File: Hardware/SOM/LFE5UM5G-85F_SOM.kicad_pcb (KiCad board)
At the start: 6 copper layers, 67.6 x 25.4 mm, 42 parts, among them J1 SODIMM-200_Split, U1 LFE5UM5G-85F, U2 AS4C256M16D3, U3 TLV62569DBV, U4 W25Q128JVP

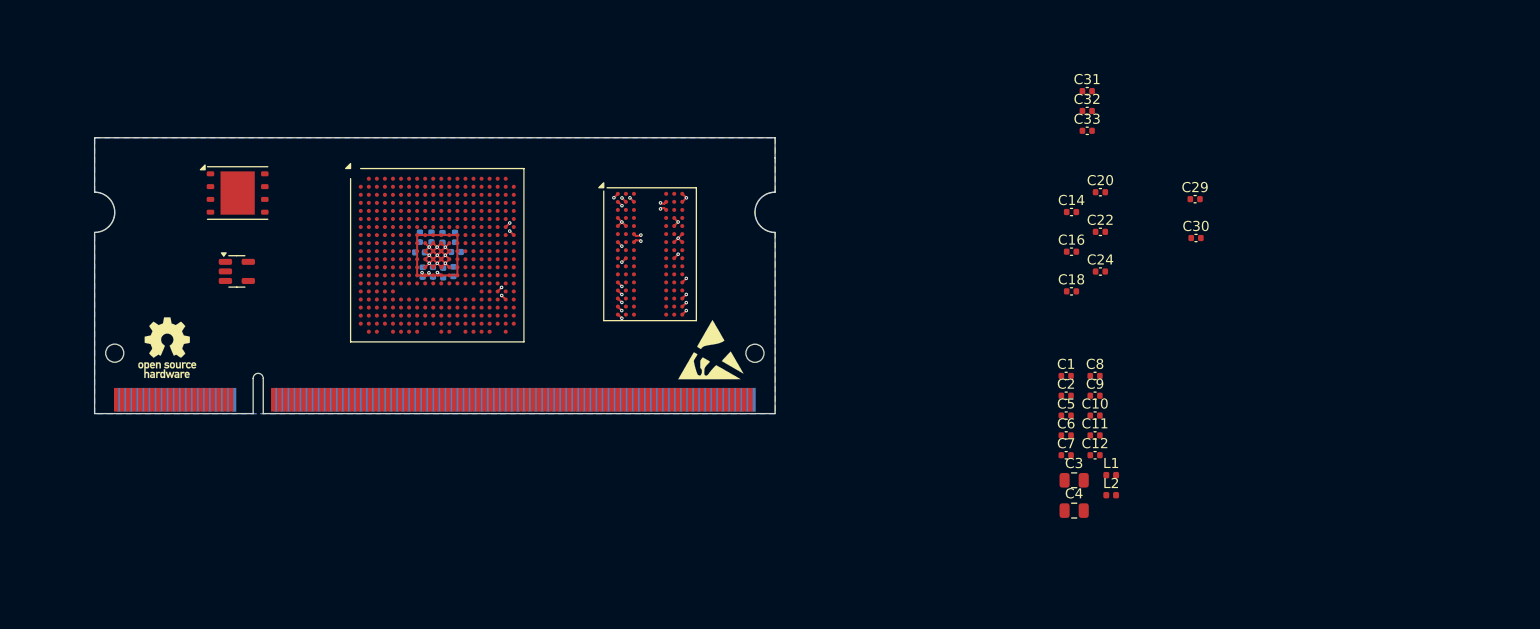
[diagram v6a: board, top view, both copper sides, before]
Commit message: SOM: power supply update
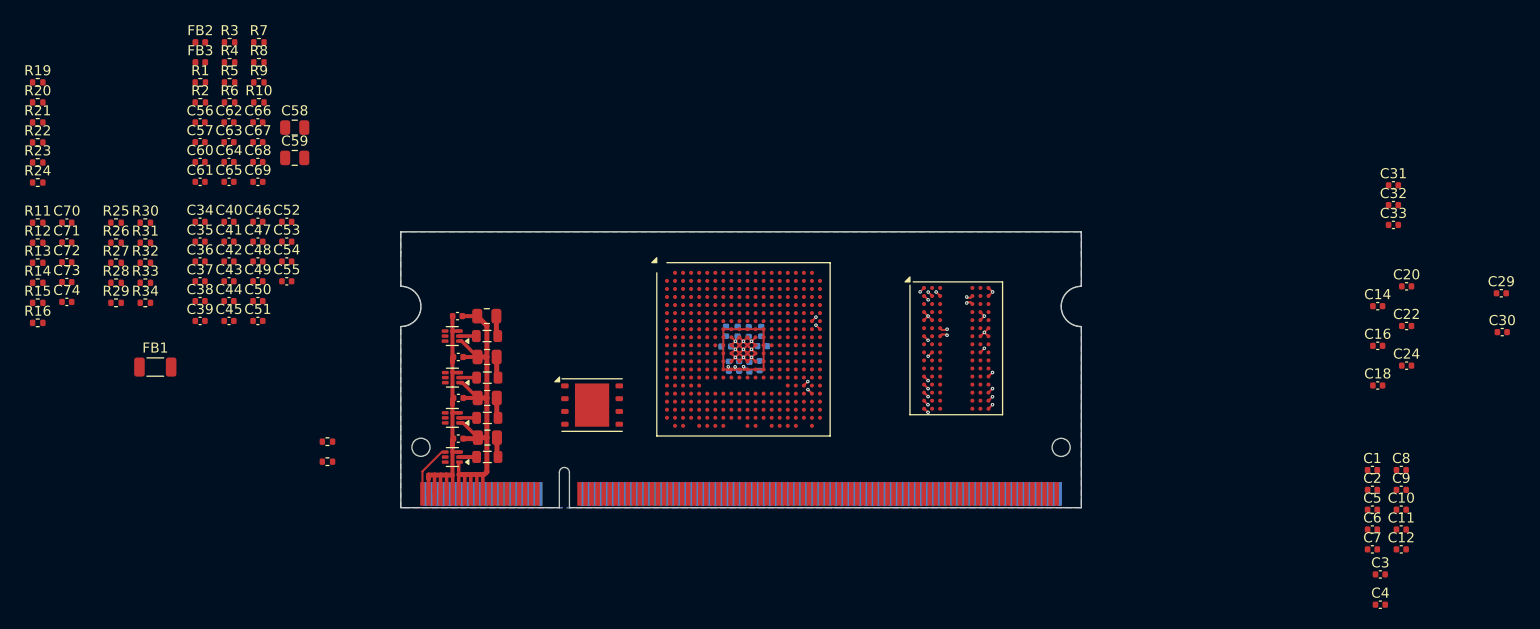
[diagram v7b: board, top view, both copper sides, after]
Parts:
- removed REF**: OSHW-Logo_5.7x6mm_SilkScreen, Symbol:OSHW-Logo_5.7x6mm_SilkScreen
- removed REF**: ESD-Logo_6.6x6mm_SilkScreen, Symbol:ESD-Logo_6.6x6mm_SilkScreen
- added C34: 100nF, Capacitor_SMD:C_0402_1005Metric, F.Cu at (61.9, 58.0)
- added C35: 10uF, Capacitor_SMD:C_0402_1005Metric, F.Cu at (61.9, 59.9)
- added C36: 10uF, Capacitor_SMD:C_0402_1005Metric, F.Cu at (61.9, 61.9)
- added C37: 10uF, Capacitor_SMD:C_0402_1005Metric, F.Cu at (61.9, 63.9)
- added C38: 10uF, Capacitor_SMD:C_0402_1005Metric, F.Cu at (61.9, 65.8)
- added C39: 10uF, Capacitor_SMD:C_0402_1005Metric, F.Cu at (61.9, 67.8)
- added C40: 1uF, Capacitor_SMD:C_0402_1005Metric, F.Cu at (64.8, 58.0)
- added C41: 100nF, Capacitor_SMD:C_0402_1005Metric, F.Cu at (64.8, 59.9)
- added C42: 100nF, Capacitor_SMD:C_0402_1005Metric, F.Cu at (64.8, 61.9)
- added C43: 1uF, Capacitor_SMD:C_0402_1005Metric, F.Cu at (64.8, 63.9)
- added C44: 100nF, Capacitor_SMD:C_0402_1005Metric, F.Cu at (64.8, 65.8)
- added C45: 100nF, Capacitor_SMD:C_0402_1005Metric, F.Cu at (64.8, 67.8)
- added C46: 100nF, Capacitor_SMD:C_0402_1005Metric, F.Cu at (67.7, 58.0)
- added C47: 100nF, Capacitor_SMD:C_0402_1005Metric, F.Cu at (67.7, 59.9)
- added C48: 1uF, Capacitor_SMD:C_0402_1005Metric, F.Cu at (67.7, 61.9)
- added C49: 100nF, Capacitor_SMD:C_0402_1005Metric, F.Cu at (67.7, 63.9)
- added C50: 100nF, Capacitor_SMD:C_0402_1005Metric, F.Cu at (67.7, 65.8)
- added C51: 100nF, Capacitor_SMD:C_0402_1005Metric, F.Cu at (67.7, 67.8)
- added C52: 100nF, Capacitor_SMD:C_0402_1005Metric, F.Cu at (70.5, 58.0)
- added C53: 100nF, Capacitor_SMD:C_0402_1005Metric, F.Cu at (70.5, 59.9)
- added C54: 10uF, Capacitor_SMD:C_0402_1005Metric, F.Cu at (70.5, 61.9)
- added C55: 10uF, Capacitor_SMD:C_0402_1005Metric, F.Cu at (70.5, 63.9)
- added C56: 100nF, Capacitor_SMD:C_0402_1005Metric, F.Cu at (61.9, 48.1)
- added C57: 100nF, Capacitor_SMD:C_0402_1005Metric, F.Cu at (61.9, 50.1)
- added C58: 22uF, Capacitor_SMD:C_0805_2012Metric, F.Cu at (71.3, 48.6)
- added C59: 22uF, Capacitor_SMD:C_0805_2012Metric, F.Cu at (71.3, 51.6)
- added C60: 1uF, Capacitor_SMD:C_0402_1005Metric, F.Cu at (61.9, 52.0)
- added C61: 1uF, Capacitor_SMD:C_0402_1005Metric, F.Cu at (61.9, 54.0)
- added C62: 1uF, Capacitor_SMD:C_0402_1005Metric, F.Cu at (64.8, 48.1)
- added C63: 1uF, Capacitor_SMD:C_0402_1005Metric, F.Cu at (64.8, 50.1)
- added C64: 100nF, Capacitor_SMD:C_0402_1005Metric, F.Cu at (64.8, 52.0)
- added C65: 100nF, Capacitor_SMD:C_0402_1005Metric, F.Cu at (64.8, 54.0)
- added C66: 100nF, Capacitor_SMD:C_0402_1005Metric, F.Cu at (67.7, 48.1)
- added C67: 100nF, Capacitor_SMD:C_0402_1005Metric, F.Cu at (67.7, 50.1)
- added C68: 1uF, Capacitor_SMD:C_0402_1005Metric, F.Cu at (67.7, 52.0)
- added C69: 100nF, Capacitor_SMD:C_0402_1005Metric, F.Cu at (67.7, 54.0)
- added C70: 22pF, Capacitor_SMD:C_0402_1005Metric, F.Cu at (48.7, 58.0)
- added C71: 22pF, Capacitor_SMD:C_0402_1005Metric, F.Cu at (48.7, 60.0)
- added C72: 22pF, Capacitor_SMD:C_0402_1005Metric, F.Cu at (48.7, 62.0)
- added C73: 100nF, Capacitor_SMD:C_0402_1005Metric, F.Cu at (48.7, 64.0)
- added C74: 10uF, Capacitor_SMD:C_0402_1005Metric, F.Cu at (48.7, 65.9)
- added C75: 10uF, Capacitor_SMD:C_0402_1005Metric, F.Cu at (87.6, 79.5)
- added C76: 10uF, Capacitor_SMD:C_0402_1005Metric, F.Cu at (87.6, 75.5)
- added C77: 22uF, Capacitor_SMD:C_0805_2012Metric, F.Cu at (90.5, 79.4)
- added C78: 22uF, Capacitor_SMD:C_0805_2012Metric, F.Cu at (90.5, 75.5)
- added C79: 10uF, Capacitor_SMD:C_0402_1005Metric, F.Cu at (87.6, 71.4)
- added C80: 10uF, Capacitor_SMD:C_0402_1005Metric, F.Cu at (87.5, 67.3)
- added C81: 22uF, Capacitor_SMD:C_0805_2012Metric, F.Cu at (90.4, 71.4)
- added C82: 22uF, Capacitor_SMD:C_0805_2012Metric, F.Cu at (90.4, 67.3)
- added FB1: FerriteBead, Inductor_SMD:L_1206_3216Metric, F.Cu at (57.5, 72.4)
- added FB2: FerriteBead, Inductor_SMD:L_0402_1005Metric, F.Cu at (62.0, 40.1)
- added FB3: FerriteBead, Inductor_SMD:L_0402_1005Metric, F.Cu at (62.0, 42.1)
- added L3: 1uH, Inductor_SMD:L_0805_2012Metric, F.Cu at (90.5, 73.5)
- added L4: 1uH, Inductor_SMD:L_0805_2012Metric, F.Cu at (90.4, 69.3)
- added R1: 100R, Resistor_SMD:R_0402_1005Metric, F.Cu at (62.0, 44.1)
- added R10: 1K, Resistor_SMD:R_0402_1005Metric, F.Cu at (67.8, 46.1)
- added R11: 49.9R, Resistor_SMD:R_0402_1005Metric, F.Cu at (45.8, 58.1)
- added R12: 4k7, Resistor_SMD:R_0402_1005Metric, F.Cu at (45.8, 60.0)
- added R13: 0R, Resistor_SMD:R_0402_1005Metric, F.Cu at (45.8, 62.0)
- added R14: 4k7, Resistor_SMD:R_0402_1005Metric, F.Cu at (45.8, 64.0)
- added R15: 1k, Resistor_SMD:R_0402_1005Metric, F.Cu at (45.8, 66.0)
- added R16: 4k7, Resistor_SMD:R_0402_1005Metric, F.Cu at (45.8, 68.0)
- added R17: 442k, Resistor_SMD:R_0402_1005Metric, F.Cu at (74.6, 79.8)
- added R18: 100K, Resistor_SMD:R_0402_1005Metric, F.Cu at (74.6, 81.8)
- added R19: 316k, Resistor_SMD:R_0402_1005Metric, F.Cu at (45.8, 44.1)
- added R2: 10K, Resistor_SMD:R_0402_1005Metric, F.Cu at (62.0, 46.1)
- added R20: 100K, Resistor_SMD:R_0402_1005Metric, F.Cu at (45.8, 46.1)
- added R21: 150k, Resistor_SMD:R_0402_1005Metric, F.Cu at (45.8, 48.1)
- added R22: 100K, Resistor_SMD:R_0402_1005Metric, F.Cu at (45.8, 50.1)
- added R23: 100K, Resistor_SMD:R_0402_1005Metric, F.Cu at (45.8, 52.1)
- added R24: 100K, Resistor_SMD:R_0402_1005Metric, F.Cu at (45.8, 54.1)
- added R25: 10K, Resistor_SMD:R_0402_1005Metric, F.Cu at (53.6, 58.1)
- added R26: 10K, Resistor_SMD:R_0402_1005Metric, F.Cu at (53.6, 60.0)
- added R27: 10K, Resistor_SMD:R_0402_1005Metric, F.Cu at (53.6, 62.0)
- added R28: 10K, Resistor_SMD:R_0402_1005Metric, F.Cu at (53.6, 64.0)
- added R29: 10K, Resistor_SMD:R_0402_1005Metric, F.Cu at (53.6, 66.0)
- added R3: 10K, Resistor_SMD:R_0402_1005Metric, F.Cu at (64.9, 40.1)
- added R30: 10K, Resistor_SMD:R_0402_1005Metric, F.Cu at (56.5, 58.1)
- added R31: 4.7k, Resistor_SMD:R_0402_1005Metric, F.Cu at (56.5, 60.0)
- added R32: 4.7k, Resistor_SMD:R_0402_1005Metric, F.Cu at (56.5, 62.0)
- added R33: 4.7k, Resistor_SMD:R_0402_1005Metric, F.Cu at (56.5, 64.0)
- added R34: 4.7k, Resistor_SMD:R_0402_1005Metric, F.Cu at (56.5, 66.0)
- added R4: 10K, Resistor_SMD:R_0402_1005Metric, F.Cu at (64.9, 42.1)
- added R5: 10K, Resistor_SMD:R_0402_1005Metric, F.Cu at (64.9, 44.1)
- added R6: 10K, Resistor_SMD:R_0402_1005Metric, F.Cu at (64.9, 46.1)
- added R7: 10K, Resistor_SMD:R_0402_1005Metric, F.Cu at (67.8, 40.1)
- added R8: 240R, Resistor_SMD:R_0402_1005Metric, F.Cu at (67.8, 42.1)
- added R9: 1K, Resistor_SMD:R_0402_1005Metric, F.Cu at (67.8, 44.1)
- added U5: TPS62A02ADRL, Package_TO_SOT_SMD:SOT-563, F.Cu at (87.0, 77.5)
- added U6: TPS62A02ADRL, Package_TO_SOT_SMD:SOT-563, F.Cu at (87.0, 73.5)
- added U7: TPS62A02ADRL, Package_TO_SOT_SMD:SOT-563, F.Cu at (87.0, 69.3)
- C10, C11, C12, C25, C26: value 100nF -> 10uF
- C18, C29, C30, C33: value 10uF -> 100nF
- C3, C4: value 22uF -> 100nF; footprint Capacitor_SMD:C_0805_2012Metric -> Capacitor_SMD:C_0402_1005Metric
- C5, C6, C7, C8: value 1uF -> 100nF
- L1, L2: value 600R -> 1uH; footprint Inductor_SMD:L_0402_1005Metric -> Inductor_SMD:L_0805_2012Metric
- U3: value TLV62569DBV -> W25Q128JVP; footprint Package_TO_SOT_SMD:SOT-23-5 -> Package_SON:WSON-8-1EP_6x5mm_P1.27mm_EP3.4x4.3mm
- U4: value W25Q128JVP -> TPS62A02ADRL; footprint Package_SON:WSON-8-1EP_6x5mm_P1.27mm_EP3.4x4.3mm -> Package_TO_SOT_SMD:SOT-563
- moved L2 62.5 mm to (90.5, 77.5)
- moved L1 62.0 mm to (90.5, 81.3)
- moved U3 37.7 mm to (100.9, 76.2)
- moved U4 33.8 mm to (87.0, 81.3), turned to 180 degrees
- moved C3 31.8 mm to (179.2, 93.0)
- moved C4 31.8 mm to (179.2, 96.0)
- moved U2 31.8 mm to (137.1, 70.5)
- moved C15 31.8 mm to (115.5, 72.3)
- moved C17 31.8 mm to (116.5, 72.4)
- moved C19 31.8 mm to (117.5, 72.3)
- moved C21 31.8 mm to (117.7, 68.9)
- moved C23 31.8 mm to (116.4, 68.9)
- moved C25 31.8 mm to (115.3, 68.8)
- moved C26 31.8 mm to (114.2, 68.8)
- moved C27 31.8 mm to (114.2, 70.4)
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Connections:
- C1 pad 2: DDR_VDDQ_1.5V -> 1.2V
- C10 pad 2: DDR_VDD_1.5V -> Net-(C10-Pad2)
- C11 pad 2: DDR_VDDQ_1.5V -> 1.5V
- C12 pad 2: DDR_VDD_1.5V -> 1.5V
- C13 pad 2: VCC_CORE -> 1.2V
- C14 pad 2: 1.5V -> 1.2V
- C15 pad 2: VCC_CORE -> Net-(C15-Pad2)
- C16 pad 2: 1.5V -> Net-(C16-Pad2)
- C17 pad 2: VCC_CORE -> Net-(C17-Pad2)
- C18 pad 2: 1.5V -> 1.2V
- C19 pad 2: VCC_CORE -> Net-(C15-Pad2)
- C2 pad 2: DDR_VDD_1.5V -> Net-(C10-Pad2)
- C20 pad 2: 1.5V -> Net-(C16-Pad2)
- C21 pad 2: VCC_CORE -> Net-(C17-Pad2)
- C22 pad 2: 1.5V -> 1.2V
- C23 pad 2: VCC_CORE -> 1.2V
- C24 pad 2: 1.5V -> Net-(C15-Pad2)
- C25 pad 2: VCC_CORE -> Net-(C16-Pad2)
- C26 pad 2: VCC_CORE -> Net-(C17-Pad2)
- C27 pad 2: VCC_CORE -> 1.2V
- C28 pad 2: VCC_CORE -> 1.5V
- C29 pad 2: VCC_CORE -> Net-(C29-Pad2)
- C3 pad 2: DDR_VDDQ_1.5V -> 1.5V
- C30 pad 2: VCC_CORE -> 3.3V
- C31 pad 2: 1.5V -> 1.2V
- C33 pad 2: 1.5V -> Net-(C29-Pad2)
- C4 pad 2: DDR_VDD_1.5V -> 1.5V
- C5 pad 2: DDR_VDDQ_1.5V -> 1.2V
- C6 pad 2: DDR_VDD_1.5V -> Net-(C10-Pad2)
- C7 pad 2: DDR_VDDQ_1.5V -> 1.5V
- C8 pad 2: DDR_VDD_1.5V -> 1.5V
- C9 pad 2: DDR_VDDQ_1.5V -> 1.2V
- J1 pad 1: unconnected-(J1-Pad1) -> BB_PGOOD
- J1 pad 11: unconnected-(J1-Pad11) -> 5V
- J1 pad 13: unconnected-(J1-Pad13) -> GND
- J1 pad 15: unconnected-(J1-Pad15) -> GND
- J1 pad 17: unconnected-(J1-Pad17) -> GND
- J1 pad 19: unconnected-(J1-Pad19) -> GND
- J1 pad 2: ANY -> unconnected-(J1-Pad2)
- J1 pad 21: unconnected-(J1-Pad21) -> GND
- J1 pad 3: unconnected-(J1-Pad3) -> 5V
- J1 pad 5: unconnected-(J1-Pad5) -> 5V
- J1 pad 7: unconnected-(J1-Pad7) -> 5V
- J1 pad 9: unconnected-(J1-Pad9) -> 5V
- L1 pad 1: VDD_1.5V -> Net-(U4-SW)
- L1 pad 2: DDR_VDDQ_1.5V -> 3.3V
- L2 pad 1: VDD_1.5V -> Net-(U5-SW)
- L2 pad 2: DDR_VDD_1.5V -> 2.5V
- U1 pad A15: DDR_A1 -> unconnected-(U1C-PT103A-PadA15)
- U1 pad A16: DDR_A6 -> unconnected-(U1C-PT110A-PadA16)
- U1 pad A17: DDR_A12 -> unconnected-(U1C-PT116A-PadA17)
- U1 pad A18: DDR_A14 -> unconnected-(U1C-PT119A-PadA18)
- U1 pad A19: DDR_BA1 -> unconnected-(U1C-PT121A-PadA19)
- U1 pad B14: Net-(U1A-GND-PadB14) -> GND
- U1 pad B15: DDR_A2 -> unconnected-(U1C-PT105A-PadB15)
- U1 pad B16: DDR_A7 -> unconnected-(U1C-PT110B-PadB16)
- U1 pad B17: DDR_A10 -> unconnected-(U1C-PT114A-PadB17)
- U1 pad B18: DDR_A13 -> unconnected-(U1C-PT116B-PadB18)
- U1 pad B19: DDR_BA0 -> unconnected-(U1C-PT119B-PadB19)
- U1 pad B20: DDR_BA2 -> unconnected-(U1C-PT121B-PadB20)
- U1 pad B7: Net-(U1A-GND-PadB14) -> GND
- U1 pad C15: DDR_A3 -> unconnected-(U1C-PT105B-PadC15)
- U1 pad C16: DDR_A8 -> unconnected-(U1C-PT112A-PadC16)
- U1 pad C17: DDR_A11 -> unconnected-(U1C-PT114B-PadC17)
- U1 pad C19: Net-(U1A-GND-PadB14) -> GND
- U1 pad D15: DDR_A4 -> unconnected-(U1C-PT107A-PadD15)
- U1 pad D16: DDR_A9 -> unconnected-(U1C-PT112B-PadD16)
- U1 pad D20: DDR_DQ10 -> DDR_VREF
- U1 pad D4: Net-(U1A-GND-PadB14) -> GND
- U1 pad E14: DDR_A0 -> unconnected-(U1C-PT85B-PadE14)
- U1 pad E15: DDR_A5 -> unconnected-(U1C-PT107B-PadE15)
- U1 pad F11: Net-(U1C-VCCIO1-PadF11) -> 1.5V
- U1 pad F12: Net-(U1C-VCCIO1-PadF11) -> 1.5V
- U1 pad F13: Net-(U1A-GND-PadB14) -> GND
- U1 pad F14: Net-(U1A-GND-PadB14) -> GND
- U1 pad F15: Net-(U1A-VCCAUX-PadF15) -> 2.5V_A
- U1 pad F17: unconnected-(U1D-PR17A-PadF17) -> DDR_CKE
- U1 pad F6: Net-(U1A-VCCAUX-PadF15) -> 2.5V_A
- U1 pad F7: Net-(U1A-GND-PadB14) -> GND
- U1 pad F8: Net-(U1A-GND-PadB14) -> GND
- U1 pad G10: Net-(U1A-GND-PadB14) -> GND
- U1 pad G11: Net-(U1A-GND-PadB14) -> GND
- U1 pad G12: Net-(U1A-GND-PadB14) -> GND
- U1 pad G13: Net-(U1A-GND-PadB14) -> GND
- U1 pad G14: Net-(U1A-GND-PadB14) -> GND
- U1 pad G15: Net-(U1A-GND-PadB14) -> GND
- U1 pad G17: Net-(U1A-GND-PadB14) -> GND
- U1 pad G18: unconnected-(U1D-PR17B-PadG18) -> DDR_NCK
- U1 pad G4: Net-(U1A-GND-PadB14) -> GND
- U1 pad G6: Net-(U1A-GND-PadB14) -> GND
- U1 pad G7: Net-(U1A-GND-PadB14) -> GND
- U1 pad G8: Net-(U1A-GND-PadB14) -> GND
- U1 pad G9: Net-(U1A-GND-PadB14) -> GND
- U1 pad H1: unconnected-(U1F-PL53C-PadH1) -> DDR_RAS
- U1 pad H10: VCC_CORE -> 1.2V
- U1 pad H11: VCC_CORE -> 1.2V
- U1 pad H12: VCC_CORE -> 1.2V
- U1 pad H13: VCC_CORE -> 1.2V
- U1 pad H19: Net-(U1A-GND-PadB14) -> GND
- U1 pad H8: VCC_CORE -> 1.2V
- U1 pad H9: VCC_CORE -> 1.2V
- U1 pad J1: unconnected-(U1F-PL53B-PadJ1) -> DDR_CS
- U1 pad J10: Net-(U1A-GND-PadB14) -> GND
- U1 pad J11: Net-(U1A-GND-PadB14) -> GND
- U1 pad J12: Net-(U1A-GND-PadB14) -> GND
- U1 pad J13: VCC_CORE -> 1.2V
- U1 pad J14: Net-(U1A-GND-PadB14) -> GND
- U1 pad J18: unconnected-(U1D-PR41C-PadJ18) -> DDR_UDM
- U1 pad J2: Net-(U1A-GND-PadB14) -> GND
- U1 pad J7: Net-(U1A-GND-PadB14) -> GND
- U1 pad J8: VCC_CORE -> 1.2V
- U1 pad J9: Net-(U1A-GND-PadB14) -> GND
- U1 pad K1: unconnected-(U1F-PL53D-PadK1) -> DDR_CAS
- U1 pad K10: Net-(U1A-GND-PadB14) -> GND
- U1 pad K11: Net-(U1A-GND-PadB14) -> GND
- U1 pad K12: Net-(U1A-GND-PadB14) -> GND
- U1 pad K13: VCC_CORE -> 1.2V
- U1 pad K14: Net-(U1A-GND-PadB14) -> GND
- U1 pad K15: Net-(U1A-GND-PadB14) -> GND
- U1 pad K18: unconnected-(U1D-PR41D-PadK18) -> DDR_DQ10
- U1 pad K2: unconnected-(U1F-PL53A-PadK2) -> DDR_RST
- U1 pad K3: unconnected-(U1F-PL50D-PadK3) -> DDR_CK
- U1 pad K4: unconnected-(U1F-PL56A-PadK4) -> DDR_WE
- U1 pad K5: unconnected-(U1F-PL56B-PadK5) -> DDR_VREF
- U1 pad K6: Net-(U1A-GND-PadB14) -> GND
- U1 pad K7: Net-(U1A-GND-PadB14) -> GND
- U1 pad K8: VCC_CORE -> 1.2V
- U1 pad K9: Net-(U1A-GND-PadB14) -> GND
- U1 pad L1: unconnected-(U1F-PL89C-PadL1) -> DDR_A12
- U1 pad L10: Net-(U1A-GND-PadB14) -> GND
- U1 pad L11: Net-(U1A-GND-PadB14) -> GND
- U1 pad L12: Net-(U1A-GND-PadB14) -> GND
- U1 pad L13: VCC_CORE -> 1.2V
- U1 pad L2: unconnected-(U1F-PL86D-PadL2) -> DDR_A9
- U1 pad L3: unconnected-(U1F-PL86C-PadL3) -> DDR_A8
- U1 pad L4: unconnected-(U1F-PL56C-PadL4) -> DDR_ODT
- U1 pad L5: unconnected-(U1F-PL56D-PadL5) -> DDR_A0
- U1 pad L6: Net-(U1F-VCCIO6-PadL6) -> 1.5V
- U1 pad L7: Net-(U1F-VCCIO6-PadL6) -> 1.5V
- U1 pad L8: VCC_CORE -> 1.2V
- U1 pad L9: Net-(U1A-GND-PadB14) -> GND
- U1 pad M1: unconnected-(U1F-PL89B-PadM1) -> DDR_A11
- U1 pad M10: Net-(U1A-GND-PadB14) -> GND
- U1 pad M11: Net-(U1A-GND-PadB14) -> GND
- U1 pad M12: Net-(U1A-GND-PadB14) -> GND
- U1 pad M13: VCC_CORE -> 1.2V
- U1 pad M14: Net-(U1A-GND-PadB14) -> GND
- U1 pad M16: Net-(U1A-GND-PadB14) -> GND
- U1 pad M2: Net-(U1A-GND-PadB14) -> GND
- U1 pad M3: unconnected-(U1F-PL86B-PadM3) -> DDR_A7
- U1 pad M4: unconnected-(U1F-PL83A-PadM4) -> DDR_A2
- U1 pad M5: unconnected-(U1F-PL77A-PadM5) -> DDR_A1
- U1 pad M6: Net-(U1F-VCCIO6-PadL6) -> 1.5V
- U1 pad M7: Net-(U1A-GND-PadB14) -> GND
- U1 pad M8: VCC_CORE -> 1.2V
- U1 pad M9: Net-(U1A-GND-PadB14) -> GND
- U1 pad N1: unconnected-(U1F-PL89D-PadN1) -> DDR_A13
- U1 pad N10: VCC_CORE -> 1.2V
- U1 pad N11: VCC_CORE -> 1.2V
- U1 pad N12: VCC_CORE -> 1.2V
- U1 pad N13: VCC_CORE -> 1.2V
- U1 pad N14: Net-(U1A-GND-PadB14) -> GND
- U1 pad N15: Net-(U1A-GND-PadB14) -> GND
- U1 pad N2: unconnected-(U1F-PL89A-PadN2) -> DDR_A10
- U1 pad N3: unconnected-(U1F-PL86A-PadN3) -> DDR_A6
- U1 pad N4: unconnected-(U1F-PL83C-PadN4) -> DDR_A4
- U1 pad N5: unconnected-(U1F-PL83B-PadN5) -> DDR_A3
- U1 pad N6: Net-(U1A-GND-PadB14) -> GND
- U1 pad N7: Net-(U1A-GND-PadB14) -> GND
- U1 pad N8: VCC_CORE -> 1.2V
- U1 pad N9: VCC_CORE -> 1.2V
- U1 pad P1: unconnected-(U1F-PL92A-PadP1) -> DDR_A14
- U1 pad P10: Net-(U1H-VCCIO8-PadP10) -> 3.3V
- U1 pad P11: Net-(U1A-GND-PadB14) -> GND
- U1 pad P12: Net-(U1A-GND-PadB14) -> GND
- U1 pad P13: Net-(U1A-GND-PadB14) -> GND
- U1 pad P14: Net-(U1A-GND-PadB14) -> GND
- U1 pad P15: Net-(U1A-VCCAUX-PadF15) -> 2.5V_A
- U1 pad P16: unconnected-(U1E-PR56B-PadP16) -> DDR_VREF
- U1 pad P2: unconnected-(U1F-PL92B-PadP2) -> DDR_BA0
- U1 pad P3: unconnected-(U1F-PL92C-PadP3) -> DDR_BA1
- U1 pad P4: unconnected-(U1F-PL92D-PadP4) -> DDR_BA2
- U1 pad P5: unconnected-(U1F-PL83D-PadP5) -> DDR_A5
- U1 pad P6: Net-(U1A-VCCAUX-PadF15) -> 2.5V_A
- U1 pad P7: Net-(U1A-GND-PadB14) -> GND
- U1 pad P8: Net-(U1A-GND-PadB14) -> GND
- U1 pad P9: Net-(U1H-VCCIO8-PadP10) -> 3.3V
- U1 pad R19: Net-(U1A-GND-PadB14) -> GND
- U1 pad R2: unconnected-(U1H-PB15A-PadR2) -> QSPI_CS
- U1 pad R4: unconnected-(U1I-CFG_2-PadR4) -> BOOT_MODE_2
- U1 pad T10: unconnected-(U1A-VCCHTX1_D0CH1-PadT10) -> Net-(U1A-VCCHTX1_D0CH1)
- U1 pad T11: unconnected-(U1A-VCCHTX0_D1CH0-PadT11) -> Net-(U1A-VCCHTX0_D0CH0)
- U1 pad T12: unconnected-(U1A-VCCHRX0_D1CH0-PadT12) -> Net-(U1A-VCCHRX0_D0CH0)
- U1 pad T13: unconnected-(U1A-VCCHRX1_D1CH1-PadT13) -> Net-(U1A-VCCHRX1_D0CH1)
- U1 pad T14: unconnected-(U1A-VCCHTX1_D1CH1-PadT14) -> Net-(U1A-VCCHTX1_D0CH1)
- U1 pad T15: Net-(U1A-VCCA1-PadT15) -> 2.5V_A
- U1 pad T4: unconnected-(U1I-CFG_1-PadT4) -> BOOT_MODE_1
- U1 pad T6: Net-(U1A-VCCA0-PadT6) -> 2.5V_A
- U1 pad T7: unconnected-(U1A-VCCHTX0_D0CH0-PadT7) -> Net-(U1A-VCCHTX0_D0CH0)
- U1 pad T8: unconnected-(U1A-VCCHRX0_D0CH0-PadT8) -> Net-(U1A-VCCHRX0_D0CH0)
- U1 pad T9: unconnected-(U1A-VCCHRX1_D0CH1-PadT9) -> Net-(U1A-VCCHRX1_D0CH1)
- U1 pad U10: Net-(U1A-GND-PadB14) -> GND
- U1 pad U11: Net-(U1A-GND-PadB14) -> GND
- U1 pad U12: Net-(U1A-GND-PadB14) -> GND
- U1 pad U13: Net-(U1A-GND-PadB14) -> GND
- U1 pad U14: Net-(U1A-GND-PadB14) -> GND
- U1 pad U15: Net-(U1A-VCCA1-PadT15) -> 2.5V_A
- U1 pad U19: unconnected-(U1E-PR89C-PadU19) -> DDR_LDM
- U1 pad U3: unconnected-(U1I-CCLK-PadU3) -> QSPI_CLK
- U1 pad U4: unconnected-(U1I-CFG_0-PadU4) -> BOOT_MODE_0
- U1 pad U6: Net-(U1A-VCCA0-PadT6) -> 2.5V_A
- U1 pad U7: Net-(U1A-GND-PadB14) -> GND
- U1 pad U8: Net-(U1A-GND-PadB14) -> GND
- U1 pad U9: Net-(U1A-GND-PadB14) -> GND
- U1 pad V10: Net-(U1A-VCCAUXA0-PadV10) -> 2.5V_A
- U1 pad V11: Net-(U1A-VCCAUXA0-PadV10) -> 2.5V_A
- U1 pad V12: Net-(U1A-GND-PadB14) -> GND
- U1 pad V13: Net-(U1A-GND-PadB14) -> GND
- U1 pad V14: Net-(U1A-GND-PadB14) -> GND
- U1 pad V15: Net-(U1A-GND-PadB14) -> GND
- U1 pad V16: Net-(U1A-GND-PadB14) -> GND
- U1 pad V17: Net-(U1A-VCCAUXA1-PadV17) -> 2.5V_A
- U1 pad V18: Net-(U1A-VCCAUXA1-PadV17) -> 2.5V_A
- U1 pad V19: Net-(U1A-GND-PadB14) -> GND
- U1 pad V2: unconnected-(U1H-PB11A-PadV2) -> QSPI_MISO/DQ1
- U1 pad V20: Net-(U1A-GND-PadB14) -> GND
- U1 pad V3: unconnected-(U1I-~{INIT}-PadV3) -> INIT#
- U1 pad V5: Net-(U1A-GND-PadB14) -> GND
- U1 pad V6: Net-(U1A-GND-PadB14) -> GND
- U1 pad V7: Net-(U1A-GND-PadB14) -> GND
- U1 pad V8: Net-(U1A-GND-PadB14) -> GND
- U1 pad V9: Net-(U1A-GND-PadB14) -> GND
- U1 pad W1: unconnected-(U1H-PB9A-PadW1) -> QSPI_RST/DQ3
- U1 pad W12: Net-(U1A-GND-PadB14) -> GND
- U1 pad W15: Net-(U1A-GND-PadB14) -> GND
- U1 pad W16: Net-(U1A-GND-PadB14) -> GND
- U1 pad W19: Net-(U1A-GND-PadB14) -> GND
- U1 pad W2: unconnected-(U1H-PB11B-PadW2) -> QSPI_MOSI/DQ0
- U1 pad W3: unconnected-(U1I-~{PROGRAM}-PadW3) -> PROGRAM#
- U1 pad W6: Net-(U1A-GND-PadB14) -> GND
- U1 pad W7: Net-(U1A-GND-PadB14) -> GND
- U1 pad Y2: unconnected-(U1H-PB9B-PadY2) -> QSPI_WP/DQ2
- U1 pad Y3: unconnected-(U1I-DONE-PadY3) -> DONE
- U2 pad L8: DDR_ZQ -> /DDR/ZQ
- U3 pad 1: unconnected-(U3-EN-Pad1) -> Net-(U3-~{CS})
- U3 pad 2: unconnected-(U3-GND-Pad2) -> QSPI_MISO/DQ1
- U3 pad 3: unconnected-(U3-SW-Pad3) -> QSPI_WP/DQ2
- U3 pad 4: unconnected-(U3-VIN-Pad4) -> GND
- U3 pad 5: unconnected-(U3-FB-Pad5) -> QSPI_MOSI/DQ0
- U4 pad 1: unconnected-(U4-~{CS}-Pad1) -> GND
- U4 pad 2: unconnected-(U4-DO/IO_{1}-Pad2) -> Net-(U4-SW)
- U4 pad 3: unconnected-(U4-~{WP}/IO_{2}-Pad3) -> 5V
- U4 pad 4: unconnected-(U4-GND-Pad4) -> BB_PGOOD
- U4 pad 5: unconnected-(U4-DI/IO_{0}-Pad5) -> Net-(U4-FB)
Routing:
- net GND: track 11.9 -> 77.8 mm, vias 15 -> 24
- net 5V: track 0.00 -> 32.5 mm
- net Net-(U1A-GND-PadB14): track 20.4 -> 0.00 mm, vias 9 -> 0
- net VCC_CORE: track 18.9 -> 0.00 mm, vias 3 -> 0
- net (no net): track 0.00 -> 18.9 mm, vias 0 -> 3
- net BB_PGOOD: track 0.00 -> 5.29 mm
- net 1.5V: track 0.00 -> 2.10 mm
- net 1.2V: track 0.00 -> 2.04 mm
- net 2.5V: track 0.00 -> 2.03 mm
- net 3.3V: track 0.00 -> 1.96 mm
- net Net-(U4-SW): track 0.00 -> 1.70 mm
- net Net-(U5-SW): track 0.00 -> 1.69 mm
- net Net-(U6-SW): track 0.00 -> 1.68 mm
- net Net-(U7-SW): track 0.00 -> 1.68 mm

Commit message: SOM: components placement
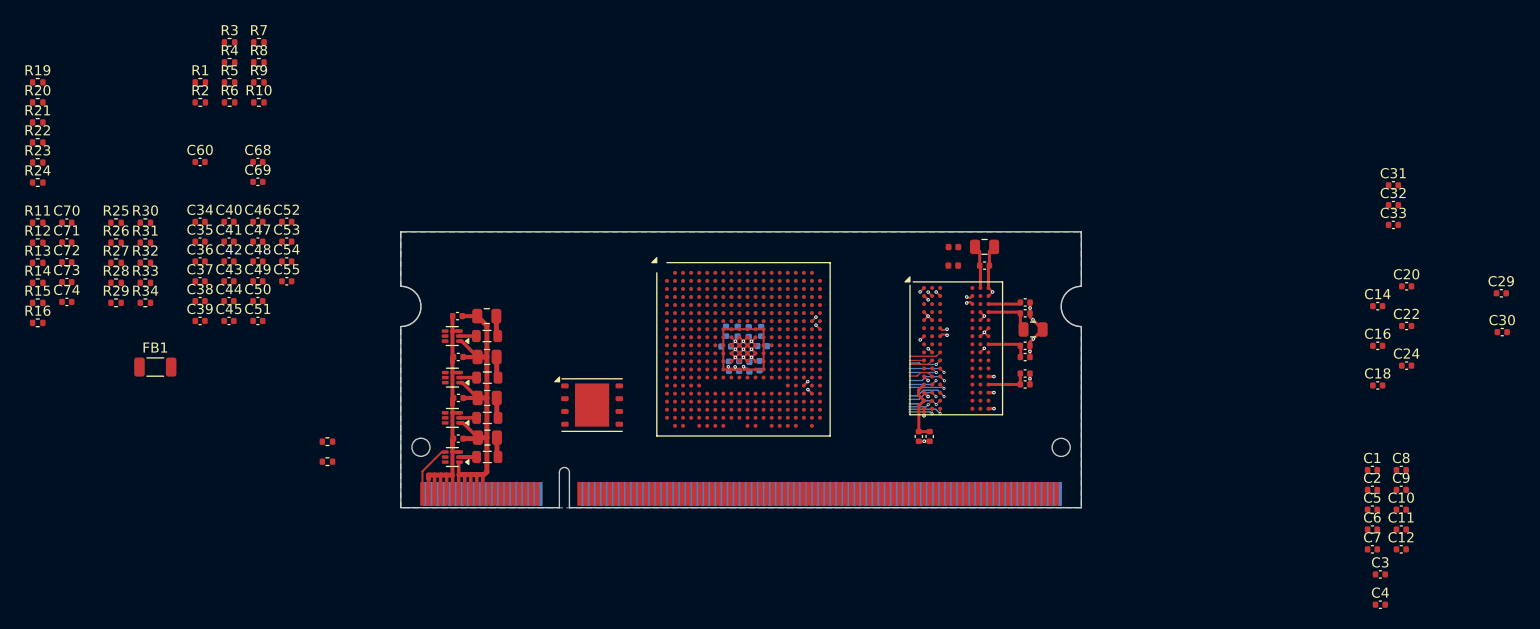
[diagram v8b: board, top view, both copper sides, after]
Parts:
- moved C57 83.7 mm to (143.9, 67.1), turned to 180 degrees
- moved C63 82.4 mm to (143.9, 73.0), turned to 180 degrees
- moved C62 82.1 mm to (143.9, 70.3), turned to 180 degrees
- moved C65 81.6 mm to (143.9, 74.1), turned to 180 degrees
- moved C64 81.4 mm to (143.9, 71.4), turned to 180 degrees
- moved C56 79.2 mm to (139.9, 62.3), turned to 180 degrees
- moved C66 78.3 mm to (143.9, 66.0), turned to 180 degrees
- moved FB2 77.5 mm to (136.8, 60.5)
- moved FB3 77.5 mm to (136.8, 62.3)
- moved C61 76.8 mm to (134.4, 79.3), turned to 90 degrees
- moved C59 75.3 mm to (144.7, 68.7), turned to 180 degrees
- moved C67 71.9 mm to (133.3, 79.3), turned to 90 degrees
- moved C58 69.5 mm to (139.9, 60.5), turned to 180 degrees
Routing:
- net DDR_VDD_1.5V: track 2.25 -> 18.6 mm, vias 4 -> 1
- net GND: track 77.8 -> 90.9 mm, vias 24 -> 30
- net DDR_VDDQ_1.5V: track 0.55 -> 12.4 mm
- net DDR_A2: track 0.00 -> 4.49 mm, vias 0 -> 1
- net DDR_BA2: track 0.00 -> 4.40 mm, vias 0 -> 1
- net DDR_WE: track 0.00 -> 4.17 mm, vias 0 -> 1
- net DDR_A0: track 0.00 -> 4.03 mm, vias 0 -> 1
- net DDR_A13: track 0.00 -> 3.79 mm, vias 0 -> 1
- net DDR_A5: track 0.00 -> 3.68 mm, vias 0 -> 1
- net DDR_A9: track 0.00 -> 3.54 mm, vias 0 -> 1
- net DDR_A3: track 0.00 -> 3.36 mm, vias 0 -> 1
- net DDR_CS: track 0.00 -> 3.29 mm, vias 0 -> 1
- net DDR_CAS: track 0.00 -> 3.26 mm, vias 0 -> 1
- net DDR_RAS: track 0.00 -> 3.20 mm
- net DDR_RST: track 0.00 -> 2.91 mm, vias 0 -> 1
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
